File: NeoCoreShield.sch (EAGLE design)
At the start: 45 parts, among them J1 PXC-PTSM-04-RA-1778641, J10 MAGJACK, J2 PXC-PTSM-04-RA-1778641, J3 PXC-PTSM-04-RA-1778641, J4 PXC-PTSM-04-RA-1778641, J5 PXC-PTSM-04-RA-1778641, Q1 2.5A/30V/105mΩ, Q2 310mA/60V/1.6Ω, Q3 2.5A/30V/105mΩ, Q4 2.5A/30V/105mΩ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

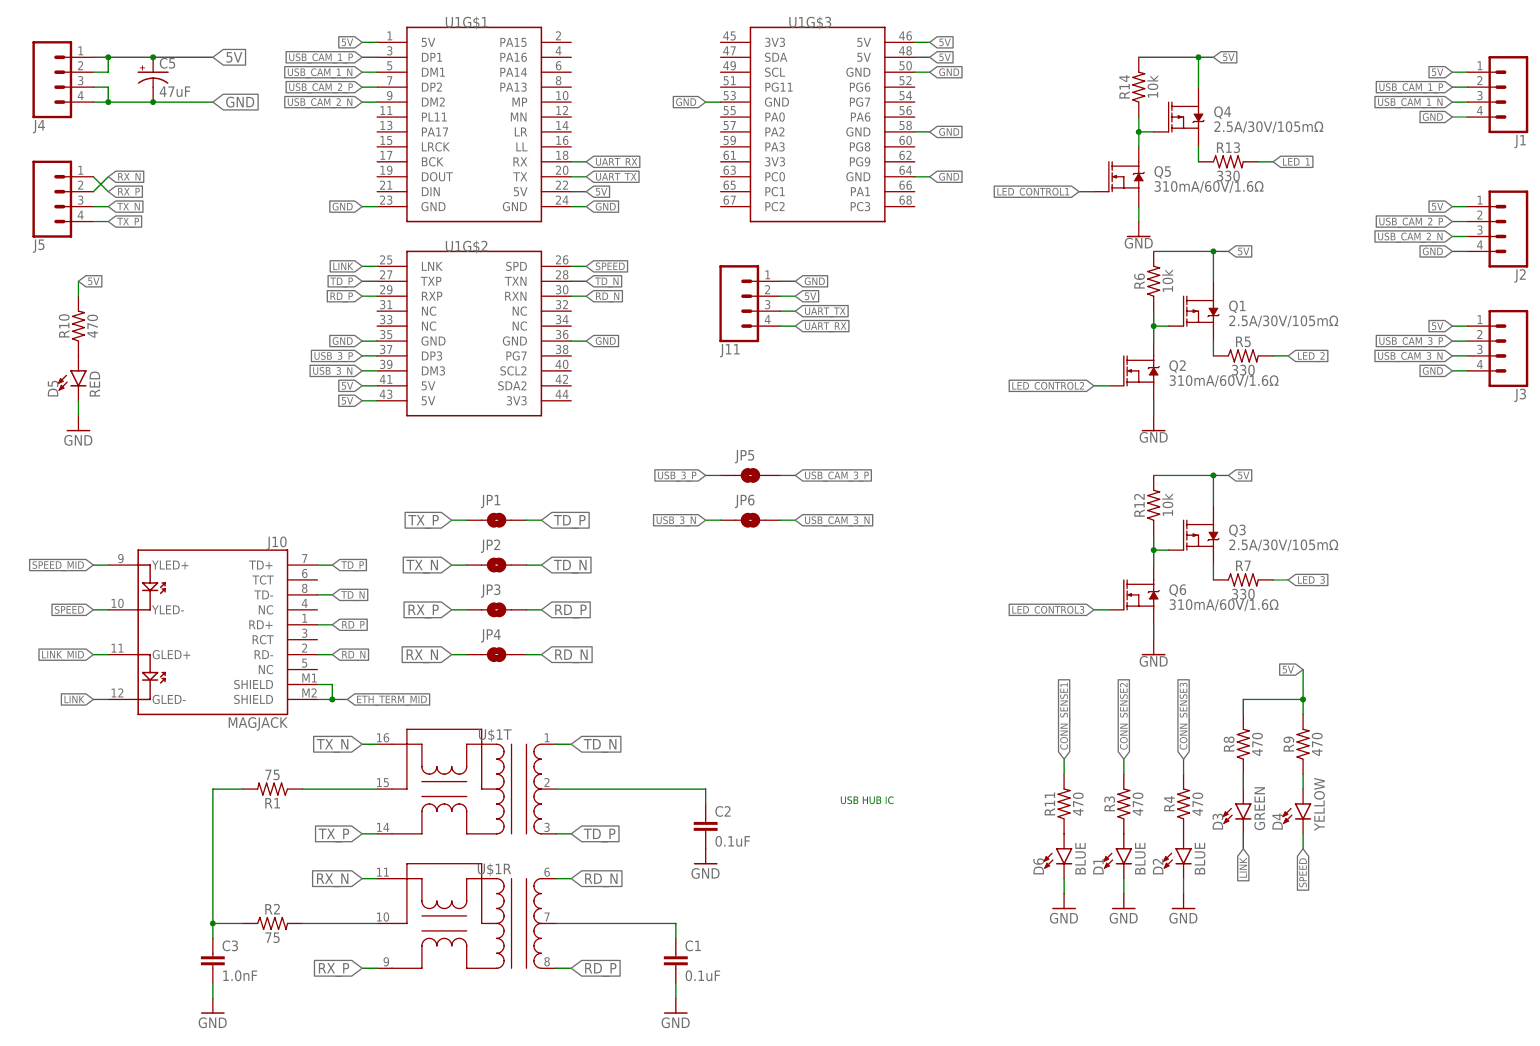
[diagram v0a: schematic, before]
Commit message: Routed Neo Core Shields
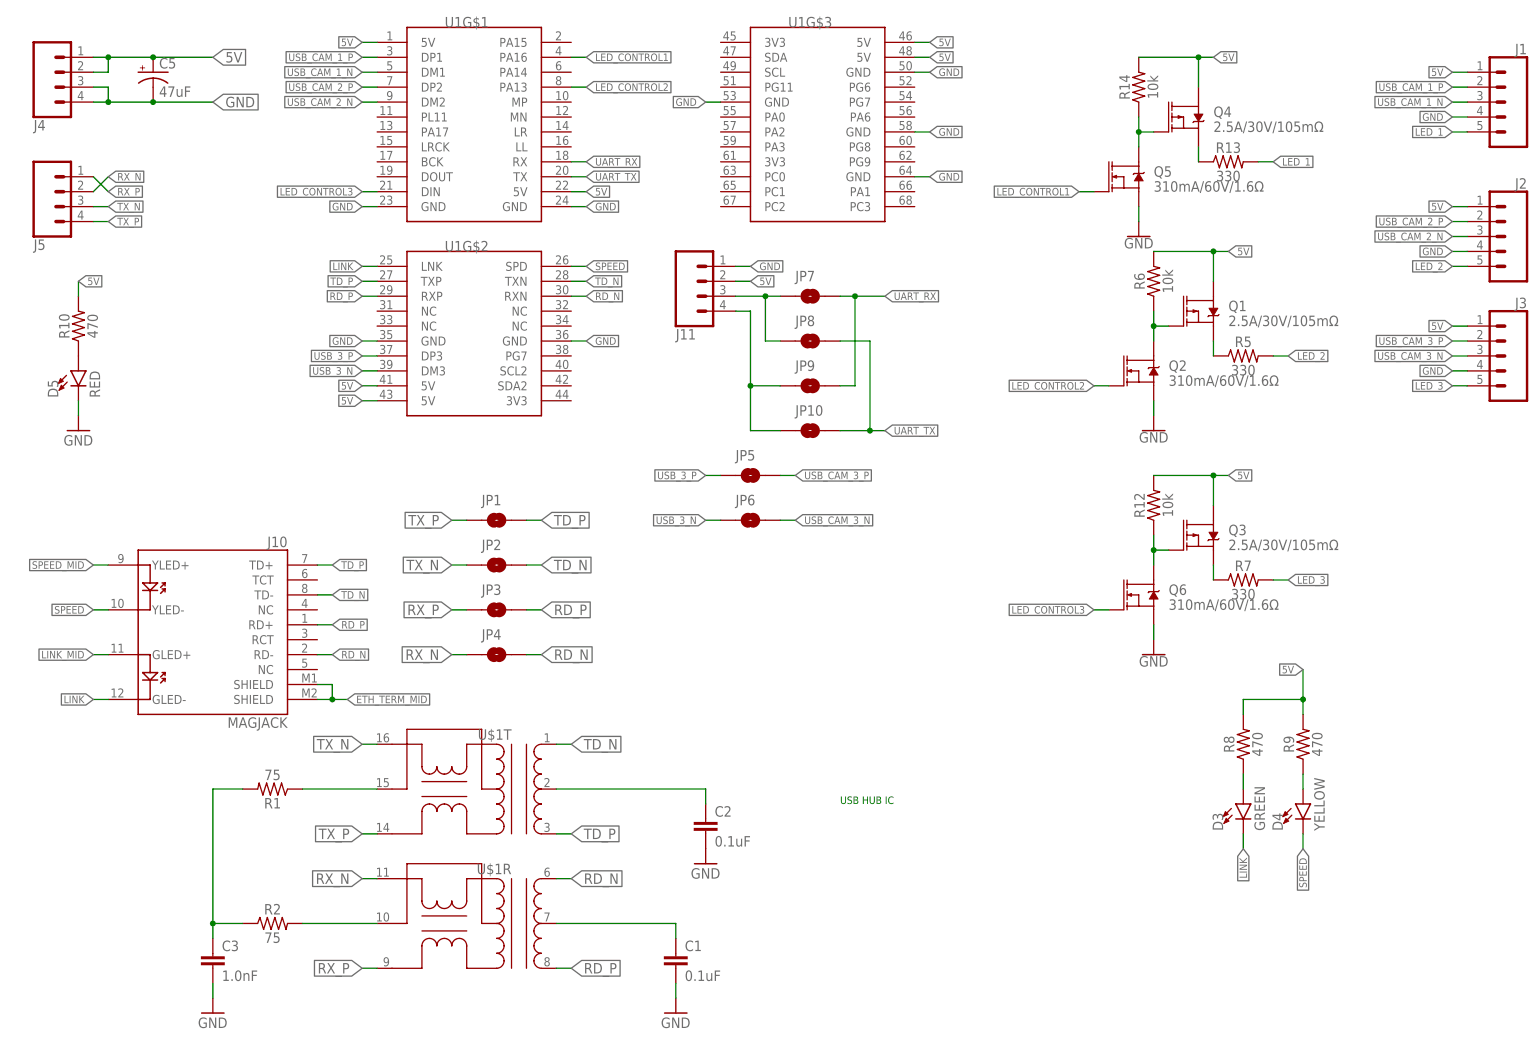
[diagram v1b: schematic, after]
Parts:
- removed D1, D2, D6: BLUE, LED-0805:LED-0805
- removed R11, R3, R4: 470, SparkFun-Resistors:0OHM-0603-1/10W-5%
- added JP10, JP7, JP8, JP9: JUMPER-SMT_2_NO_SILK, SparkFun-Jumpers:JUMPER-SMT_2_NO_SILK
- J1, J2, J3: value PXC-PTSM-04-RA-1778641 -> PXC-PTSM-05-RA; device Phoenix Contact PTSM-04-V-1778573:PXC-PTSM-04-RA-1778641 -> Phoenix Contact PTSM 5 pin:PXC-PTSM-05-RA
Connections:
- removed net CONN_SENSE1: R11.2
- removed net CONN_SENSE2: R3.2
- removed net CONN_SENSE3: R4.2
- removed net N$1: D1.A, R3.1
- removed net N$2: D2.A, R4.1
- removed net N$4: D6.A, R11.1
- new net UART_RX_TX: J11.3, JP7.1, JP8.1
- new net UART_TX_RX: J11.4, JP10.1, JP9.1
- net GND: no longer D1.C, D2.C, D6.C
- net LED_1: now also J1.5
- net LED_2: now also J2.5
- net LED_3: now also J3.5
- net LED_CONTROL1: now also U1G$1.PA16
- net LED_CONTROL2: now also U1G$1.PA13
- net LED_CONTROL3: now also U1G$1.DIN
- net UART_RX: now also JP7.2, JP9.2; no longer J11.4
- net UART_TX: now also JP10.2, JP8.2; no longer J11.3
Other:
- moved on the sheet: J11
